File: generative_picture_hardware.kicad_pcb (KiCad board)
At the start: 2 copper layers, 100 x 100 mm, 73 parts, among them J1 e_Paper_HAT, J2 Conn_ARM_JTAG_SWD_10, J3 USB_C_Receptacle_USB2.0, Q1 PMN48XP, Q2 DMG9926UDM, Q3 MBT3904DW1, SW1 SW_Push, SW2 SW_Push, U1 AP2112K-3.3, U2 ESP32-WROOM-32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

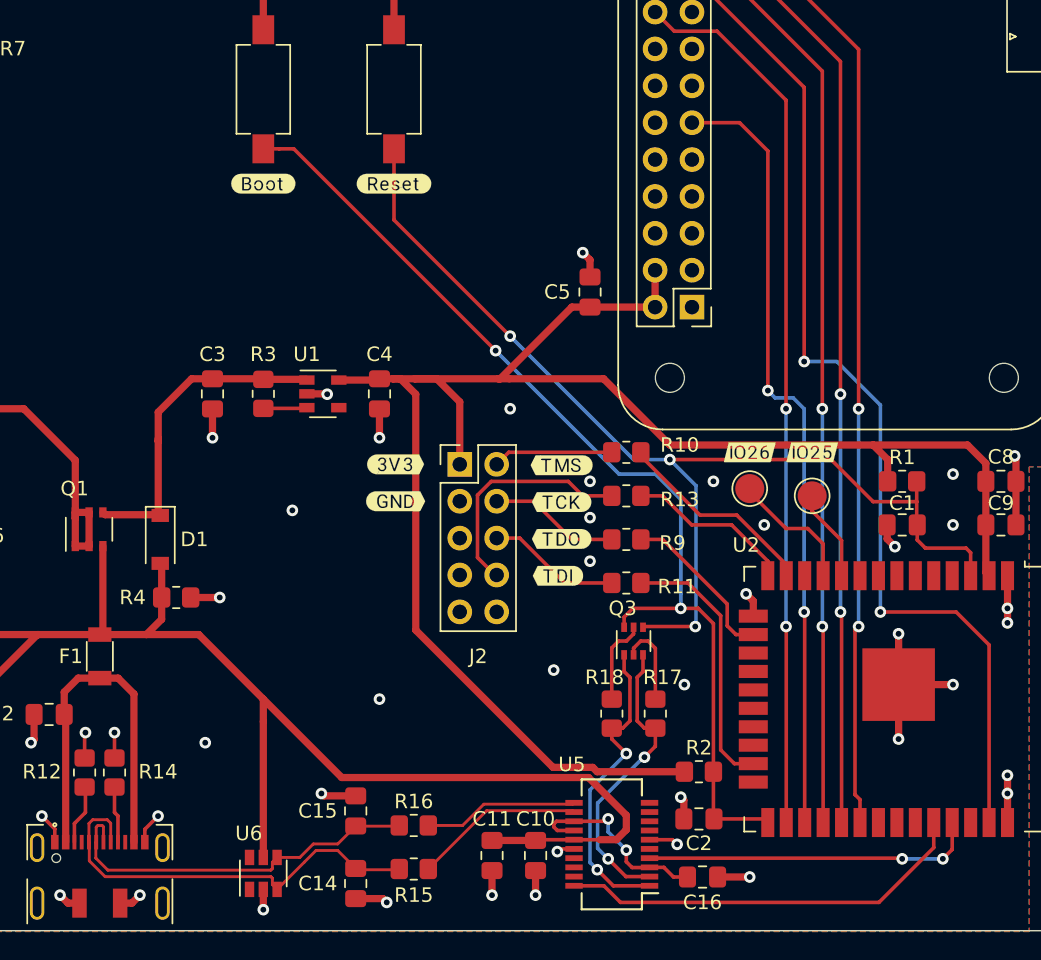
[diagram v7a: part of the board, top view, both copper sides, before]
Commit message: Brings FTDI chip closer to the usb plug
This shortens the differential pair track lenghts.
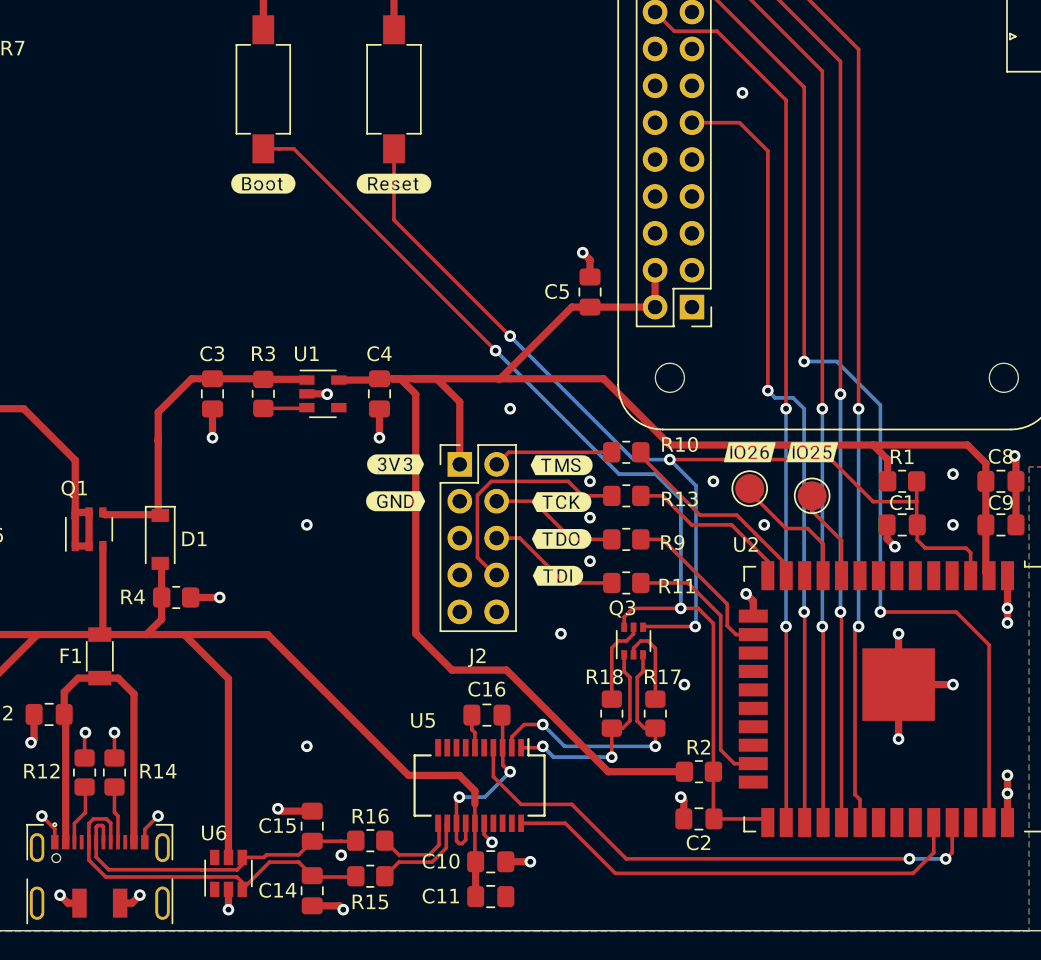
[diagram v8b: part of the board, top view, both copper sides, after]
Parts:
- moved C16 18.6 mm to (156.4, 137.1), turned to 180 degrees
- moved U5 9.97 mm to (155.9, 141.9), turned to -90 degrees
- moved C15 3.17 mm to (144.4, 144.8)
- moved R16 3.17 mm to (148.4, 145.8)
- moved C10 3.12 mm to (156.7, 147.2), turned to 0 degrees
- moved C14 3.04 mm to (144.4, 149.2)
- moved R15 3.04 mm to (148.4, 148.2)
- moved C11 2.83 mm to (156.7, 149.6), turned to 0 degrees
- moved U6 2.40 mm to (138.6, 148.0)
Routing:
- net ESP_TX: track 23.0 -> 38.2 mm
- net +5V: track 108.2 -> 99.4 mm
- net DTR: track 21.6 -> 14.8 mm
- net /USBD-: track 11.7 -> 6.77 mm
- net /USBD+: track 10.7 -> 5.94 mm
- net ESP_RX: track 28.5 -> 32.5 mm
- net /D+: track 26.6 -> 23.1 mm
- net /D-: track 29.7 -> 26.3 mm
- net GND: track 82.5 -> 79.2 mm, vias 56 -> 54
- net RTS: track 20.5 -> 19.0 mm
